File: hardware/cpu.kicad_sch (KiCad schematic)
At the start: 15 parts, among them J11 FTSH-105-01-L-DV-007-K-TR, U3 MCXA153VLH

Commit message: Wip carte alamk pwr 2.0 prete pour tirage
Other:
- note added: "Connecteur Debug ARM-SWD"
- note added: "Decouplage MCU Une capa par pin VDD"
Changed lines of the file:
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@@
+		)
+	)
+	(polyline
+		(pts
+			(xy 190.5 129.54) (xy 283.21 129.54)
+		)
+		(stroke
+			(width 0)
+			(type dash)
 		)
 	)
@@
 		)
 	)
+	(polyline
+		(pts
+			(xy 190.5 73.66) (xy 190.5 165.1)
+		)
+		(stroke
+			(width 0)
+			(type dash)
+		)
+	)
 	(wire
 		(pts
@@
 		)
 	)
+	(polyline
+		(pts
+			(xy 283.21 73.66) (xy 190.5 73.66)
+		)
+		(stroke
+			(width 0)
+			(type dash)
+		)
+	)
 	(wire
 		(pts
@@
 	(wire
 		(pts
+			(xy 187.96 24.13) (xy 187.96 26.67)
+		)
+		(stroke
+			(width 0)
+			(type default)
+		)
+	)
+	(wire
+		(pts
 			(xy 166.37 34.29) (xy 173.99 34.29)
 		)
@@
 			(width 0)
 			(type default)
+		)
+	)
+	(text "Decouplage MCU\nUne capa par pin VDD"
+		(exclude_from_sim no)
+		(at 260.35 134.62 0)
+		(effects
+			(font
+				(size 1.27 1.27)
+			)
+			(justify left)
+		)
+	)
+	(text "Connecteur \nDebug ARM-SWD"
+		(exclude_from_sim no)
+		(at 265.684 125.222 0)
+		(effects
+			(font
+				(size 1.27 1.27)
+			)
+			(justify left)
 		)
 	)
@@
 					(unit 1)
 				)
+			)
+		)
+	)
+	(symbol
+		(lib_id "power:PWR_FLAG")
+		(at 187.96 24.13 0)
+		(mirror y)
+		(unit 1)
+		(exclude_from_sim no)
+		(in_bom yes)
+		(on_board yes)
+		(dnp no)
+		(property "Reference" "#FLG5"
+			(at 187.96 22.225 0)
+			(effects
+				(font
+					(size 1.27 1.27)
+				)
+				(hide yes)
+			)
+		)
+		(property "Value" "PWR_FLAG"
+			(at 187.96 19.7104 0)
+			(effects
+				(font
+					(size 1.27 1.27)
+				)
+			)
+		)
+		(property "Footprint" ""
+			(at 187.96 24.13 0)
+			(effects
+				(font
+					(size 1.27 1.27)
+				)
+				(hide yes)
+			)
+		)
+		(property "Datasheet" "~"
+			(at 187.96 24.13 0)
+			(effects
+				(font
+					(size 1.27 1.27)
+				)
+				(hide yes)
+			)
+		)
+		(property "Description" ""
+			(at 187.96 24.13 0)
+			(effects
+				(font
+					(size 1.27 1.27)
+				)
+				(hide yes)
+			)
+		)
+		(pin "1"
+		)
+		(instances
+			(project "Carte_puissance"
+				(path "/aaa0f7a4-a021-413b-80cf-aab59bb3339a/4ebf8b14-4fd3-46f9-9345-d294b03d40c9"
+					(reference "#FLG5")
+					(unit 1)
+				)

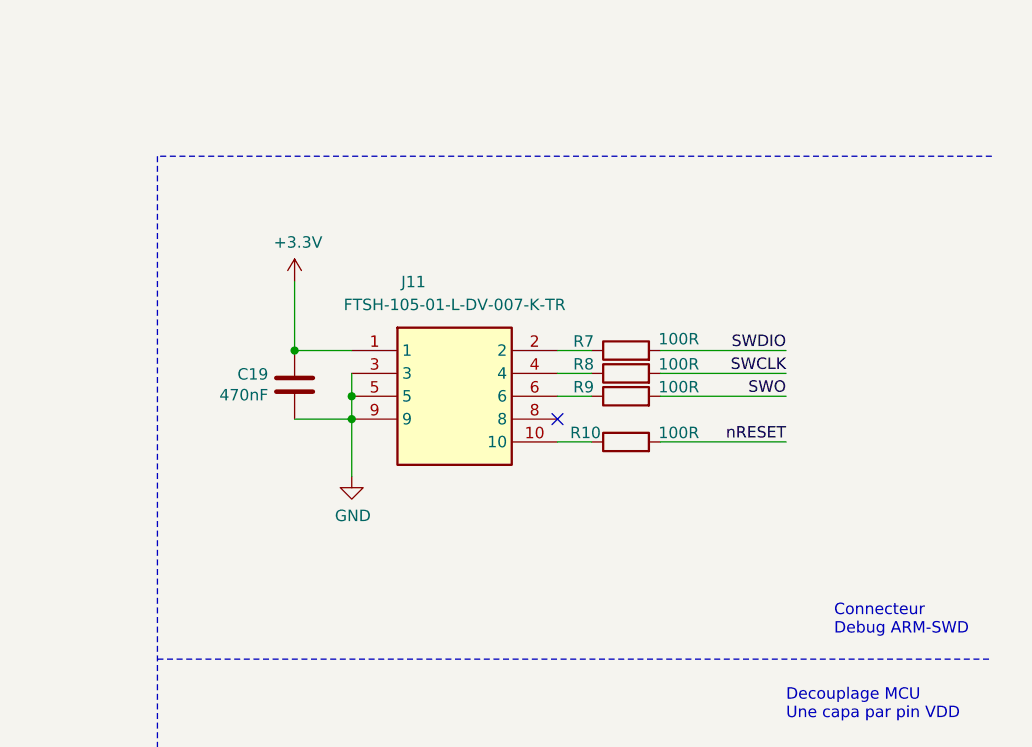
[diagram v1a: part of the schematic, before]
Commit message: Wip correction sur le connecteur debug et realisation d'un soft de test pour verifier le mapping des fonctions sur les pins
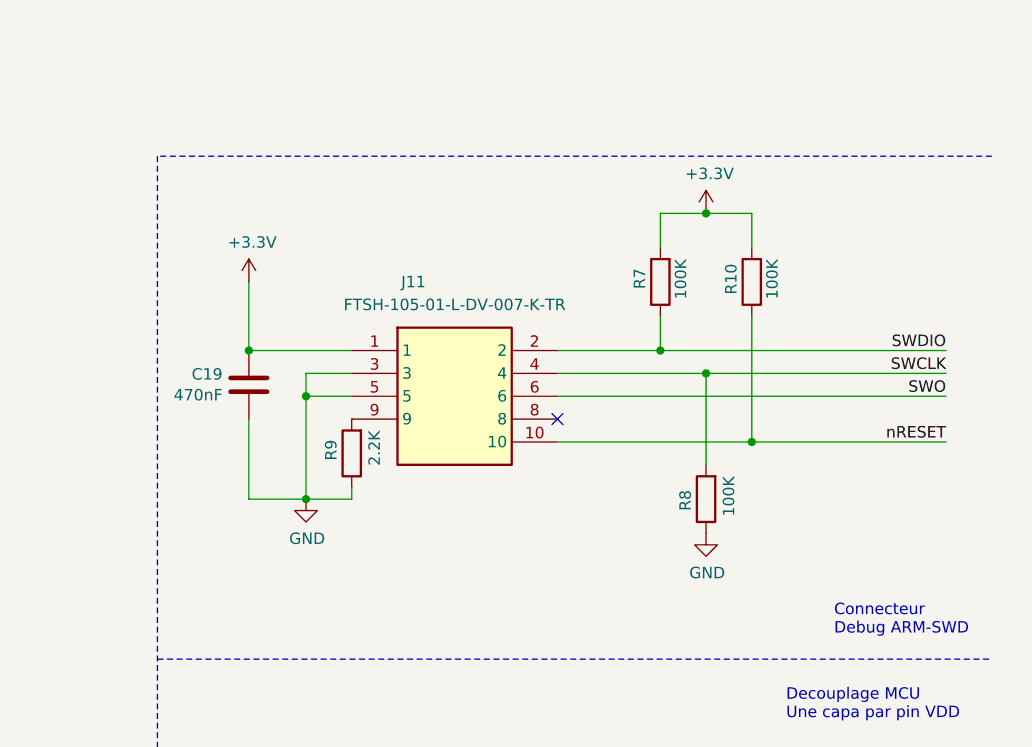
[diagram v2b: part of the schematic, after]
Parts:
- R10, R7, R8: value 100R -> 100K
- R9: value 100R -> 2.2K
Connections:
- net +3.3V: now also R10.2, R7.2
- net GND: now also R8.1, R9.1; no longer J11.9
- net SWCLK: now also J11.4
- net SWDIO: now also J11.2, R7.1; no longer R7.2
- net SWO: now also J11.6; no longer R9.2
- net nRESET: now also J11.10, R10.1; no longer R10.2
- new net: J11.9, R9.2
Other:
- moved on the sheet: C19
